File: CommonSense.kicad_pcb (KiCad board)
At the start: 2 copper layers, 35 x 24 mm, 36 parts, among them J1 Conn_02x04_Counter_Clockwise, J2 Conn_01x02, J3 Conn_01x02, J5 Conn_ARM_SWD_TagConnect_TC203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, U1 NRF52810-QFAA-R7, U2 SHT41-AD1B-R2, Y1 ECS-.327-12.5-12R-TR, Y2 ABM11W-32.0000MHZ-7-D1X-T3

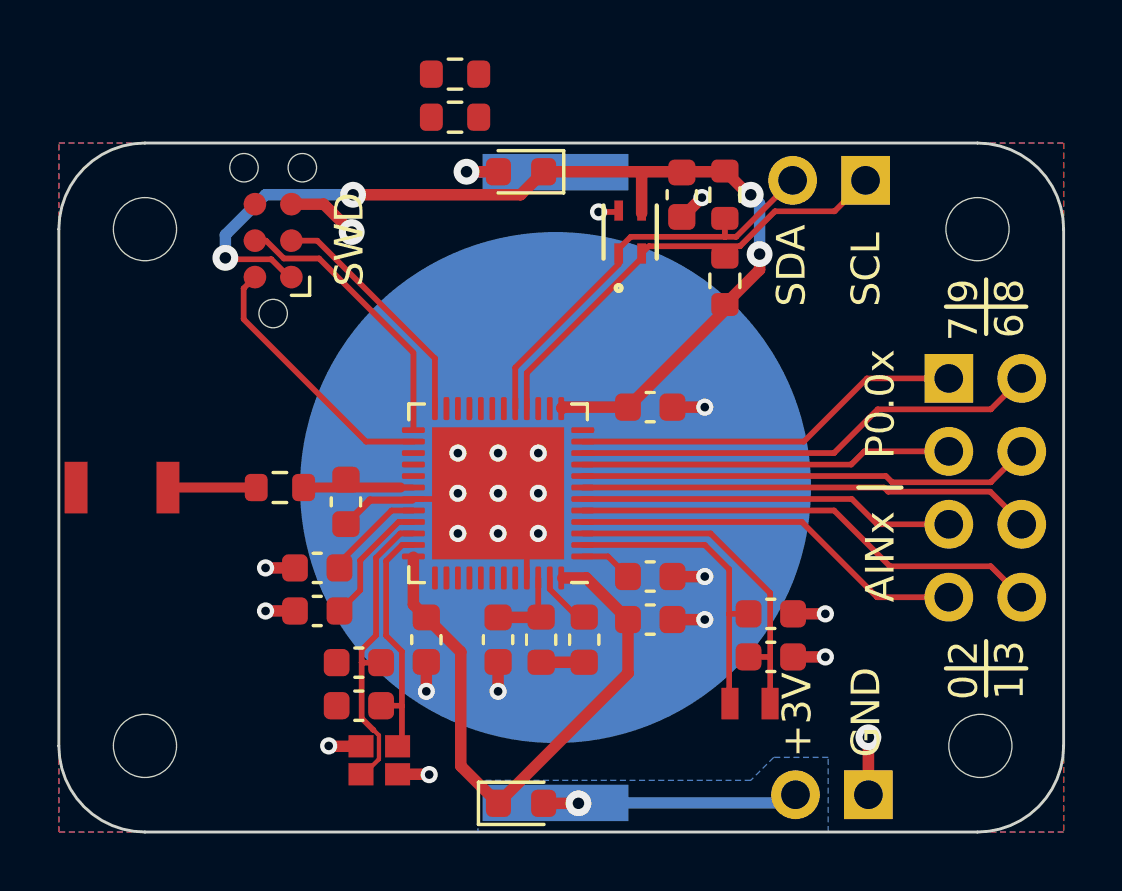
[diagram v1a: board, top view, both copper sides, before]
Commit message: Add additional 1u bypass capacitor
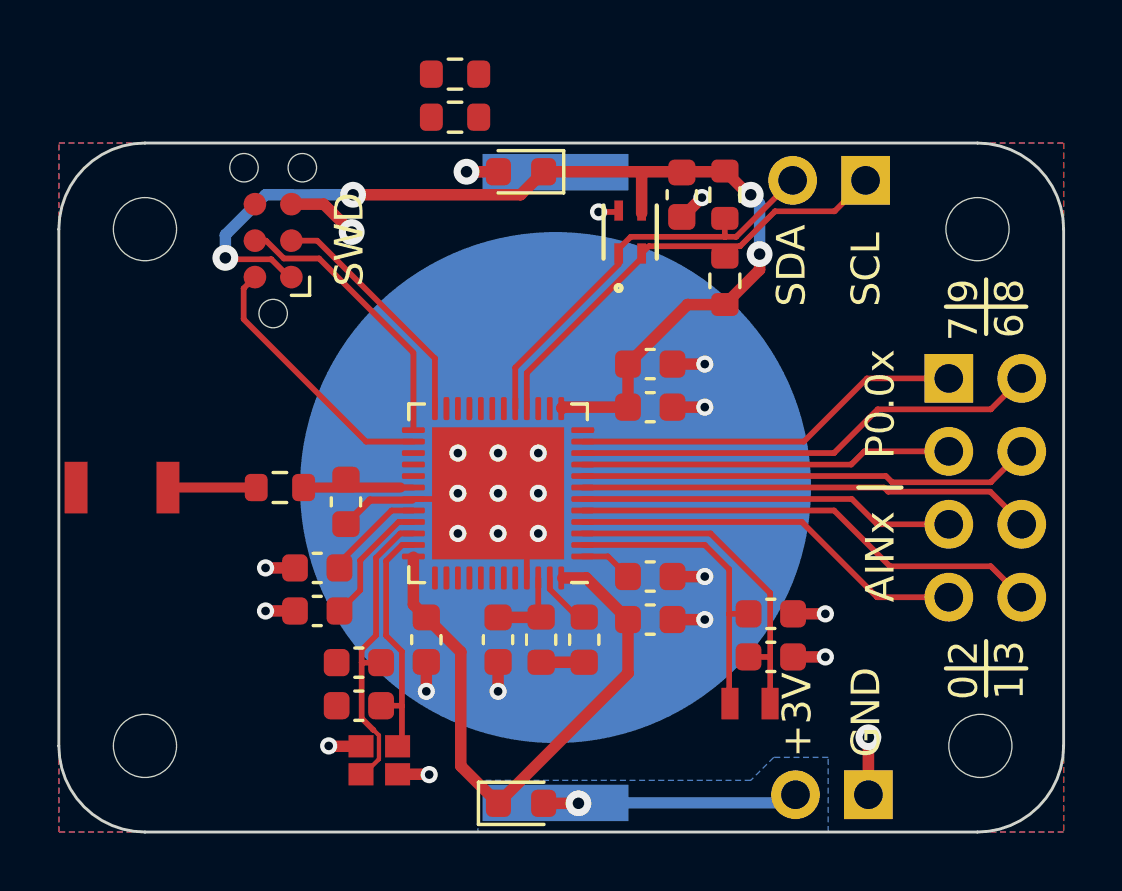
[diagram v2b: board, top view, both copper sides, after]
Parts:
- added C14: 1u, Capacitor_SMD:C_0603_1608Metric, F.Cu at (156.6, 63.7)
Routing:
- net GND: track 25.8 -> 26.9 mm, vias 24 -> 25
- net +3V0: track 57.1 -> 57.9 mm
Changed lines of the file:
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@@
+  )
+  (footprint "Capacitor_SMD:C_0603_1608Metric" (layer "F.Cu")
+    (at 156.6 63.7 180)
+    (descr "Capacitor SMD 0603 (1608 Metric), square (rectangular) end terminal, IPC_7351 nominal, (Body size source: IPC-SM-782 page 76, https://www.pcb-3d.com/wordpress/wp-content/uploads/ipc-sm-782a_amendment_1_and_2.pdf), generated with kicad-footprint-generator")
+    (tags "capacitor")
+    (property "Sheetfile" "CommonSense.kicad_sch")
+    (property "Sheetname" "")
+    (property "ki_description" "Unpolarized capacitor")
+    (property "ki_keywords" "cap capacitor")
+    (attr smd)
+    (fp_text reference "C14" (at 0 -1.43) (layer "F.SilkS") hide
+        (effects (font (size 1 1) (thickness 0.15)))
+    )
+    (fp_text value "1u" (at 0 1.43) (layer "F.Fab") hide
+        (effects (font (size 1 1) (thickness 0.15)))
+    )
+    (fp_text user "${REFERENCE}" (at 0 0) (layer "F.Fab") hide
+        (effects (font (size 0.4 0.4) (thickness 0.06)))
+    )
+    (fp_line (start -0.14058 -0.51) (end 0.14058 -0.51)
+      (stroke (width 0.12) (type solid)) (layer "F.SilkS"))
+    (fp_line (start -0.14058 0.51) (end 0.14058 0.51)
+      (stroke (width 0.12) (type solid)) (layer "F.SilkS"))
+    (fp_line (start -1.48 -0.73) (end 1.48 -0.73)
+      (stroke (width 0.05) (type solid)) (layer "F.CrtYd"))
+    (fp_line (start -1.48 0.73) (end -1.48 -0.73)
+      (stroke (width 0.05) (type solid)) (layer "F.CrtYd"))
+    (fp_line (start 1.48 -0.73) (end 1.48 0.73)
+      (stroke (width 0.05) (type solid)) (layer "F.CrtYd"))
+    (fp_line (start 1.48 0.73) (end -1.48 0.73)
+      (stroke (width 0.05) (type solid)) (layer "F.CrtYd"))
+    (fp_line (start -0.8 -0.4) (end 0.8 -0.4)
+      (stroke (width 0.1) (type solid)) (layer "F.Fab"))
+    (fp_line (start -0.8 0.4) (end -0.8 -0.4)
+      (stroke (width 0.1) (type solid)) (layer "F.Fab"))
+    (fp_line (start 0.8 -0.4) (end 0.8 0.4)
+      (stroke (width 0.1) (type solid)) (layer "F.Fab"))
+    (fp_line (start 0.8 0.4) (end -0.8 0.4)
+      (stroke (width 0.1) (type solid)) (layer "F.Fab"))
+    (pad "1" smd roundrect (at -0.775 0 180) (size 0.9 0.95) (layers "F.Cu" "F.Paste" "F.Mask") (roundrect_rratio 0.25)
+      (net 2 "GND") (pintype "passive"))
+    (pad "2" smd roundrect (at 0.775 0 180) (size 0.9 0.95) (layers "F.Cu" "F.Paste" "F.Mask") (roundrect_rratio 0.25)
+      (net 50 "+3V0") (pintype "passive"))
+    (model "${KICAD6_3DMODEL_DIR}/Capacitor_SMD.3dshapes/C_0603_1608Metric.wrl"
+      (offset (xyz 0 0 0))
+      (scale (xyz 1 1 1))
+      (rotate (xyz 0 0 0))
+    )
   )
   (footprint "Capacitor_SMD:C_0603_1608Metric" (layer "F.Cu")
@@
   (segment (start 161.575 73.9) (end 162.7 73.9) (width 0.4) (layer "F.Cu") (net 2))
   (segment (start 155.45305 58.4) (end 155.49995 58.3531) (width 0.2) (layer "F.Cu") (net 2))
+  (segment (start 157.375 63.7) (end 158.5 63.7) (width 0.4) (layer "F.Cu") (net 2))
   (segment (start 157.725 58.575) (end 158.4 57.9) (width 0.4) (layer "F.Cu") (net 2))
   (segment (start 145.413 77.013) (end 145.4 77) (width 0.4) (layer "F.Cu") (net 2))
@@
   (via (at 158.5 71.1) (size 0.6) (drill 0.3) (layers "F.Cu" "B.Cu") (net 2))
   (via (at 146.2 59.1) (size 0.9) (drill 0.4) (layers "F.Cu" "B.Cu") (net 2))
+  (via (at 158.5 63.7) (size 0.6) (drill 0.3) (layers "F.Cu" "B.Cu") (net 2))
   (via (at 148.9 78) (size 0.6) (drill 0.3) (layers "F.Cu" "B.Cu") (net 2))
   (via (at 149.9 68.2) (size 0.6) (drill 0.3) (layers "F.Cu" "B.Cu") (net 2))
@@
   (segment (start 153.285 57) (end 153.3 57.015) (width 0.4) (layer "B.Cu") (net 49))
   (segment (start 153.3 78.985) (end 161.375 78.985) (width 0.4) (layer "B.Cu") (net 49))
+  (segment (start 153.55 65.2) (end 153.527 65.223) (width 0.4) (layer "F.Cu") (net 50))
   (segment (start 143.401852 60.0493) (end 141.8493 60.0493) (width 0.2) (layer "F.Cu") (net 50))
   (segment (start 148.35 72.075) (end 148.35 70.427) (width 0.4) (layer "F.Cu") (net 50))
   (segment (start 160.409948 60.415052) (end 159.2 61.625) (width 0.4) (layer "F.Cu") (net 50))
+  (segment (start 155.825 63.7) (end 155.825 65.2) (width 0.4) (layer "F.Cu") (net 50))
+  (segment (start 153.527 65.223) (end 153.527 65.25) (width 0.4) (layer "F.Cu") (net 50))
   (segment (start 156.3 57) (end 159.175 57) (width 0.4) (layer "F.Cu") (net 50))
   (segment (start 154.375 71.15) (end 153.552 71.15) (width 0.4) (layer "F.Cu") (net 50))
+  (segment (start 159.2 61.625) (end 157.9 61.625) (width 0.4) (layer "F.Cu") (net 50))
   (segment (start 160.026642 57.801642) (end 159.2 56.975) (width 0.4) (layer "F.Cu") (net 50))
   (segment (start 156.3001 58.4531) (end 156.3001 57.0001) (width 0.4) (layer "F.Cu") (net 50))
   (segment (start 150 77.7) (end 150 73.725) (width 0.4) (layer "F.Cu") (net 50))
-  (segment (start 159.2 61.625) (end 159.2 61.825) (width 0.4) (layer "F.Cu") (net 50))
-  (segment (start 153.55 65.2) (end 153.527 65.223) (width 0.4) (layer "F.Cu") (net 50))
   (segment (start 148.8 72.525) (end 148.35 72.075) (width 0.4) (layer "F.Cu") (net 50))
   (segment (start 155.825 74.475) (end 155.825 72.6) (width 0.4) (layer "F.Cu") (net 50))
@@
   (segment (start 156.3001 57.0001) (end 156.3 57) (width 0.4) (layer "F.Cu") (net 50))
   (segment (start 152.8875 57) (end 156.3 57) (width 0.4) (layer "F.Cu") (net 50))
+  (segment (start 157.9 61.625) (end 155.825 63.7) (width 0.4) (layer "F.Cu") (net 50))
   (segment (start 160.101642 57.801642) (end 160.026642 57.801642) (width 0.4) (layer "F.Cu") (net 50))
-  (segment (start 159.2 61.825) (end 155.825 65.2) (width 0.4) (layer "F.Cu") (net 50))
   (segment (start 144.022552 60.67) (end 143.401852 60.0493) (width 0.2) (layer "F.Cu") (net 50))
   (segment (start 146.247897 57.802) (end 152.0855 57.802) (width 0.4) (layer "F.Cu") (net 50))
   (segment (start 152.0855 57.802) (end 152.8875 57) (width 0.4) (layer "F.Cu") (net 50))
-  (segment (start 155.825 65.2) (end 153.55 65.2) (width 0.4) (layer "F.Cu") (net 50))
   (segment (start 159.175 57) (end 159.2 56.975) (width 0.4) (layer "F.Cu") (net 50))
-  (segment (start 153.527 65.223) (end 153.527 65.25) (width 0.4) (layer "F.Cu") (net 50))
   (segment (start 150 73.725) (end 148.8 72.525) (width 0.4) (layer "F.Cu") (net 50))
   (segment (start 141.8493 60.0493) (end 141.8 60) (width 0.2) (layer "F.Cu") (net 50))
@@
   (segment (start 155.825 72.6) (end 154.375 71.15) (width 0.4) (layer "F.Cu") (net 50))
   (segment (start 151.3 79) (end 155.825 74.475) (width 0.4) (layer "F.Cu") (net 50))
+  (segment (start 155.825 65.2) (end 153.55 65.2) (width 0.4) (layer "F.Cu") (net 50))
   (via (at 160.409948 59.869216) (size 0.9) (drill 0.4) (layers "F.Cu" "B.Cu") (net 50))
   (via (at 160.101642 57.801642) (size 0.9) (drill 0.4) (layers "F.Cu" "B.Cu") (net 50))

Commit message: Route LED and fix silk screen warnings
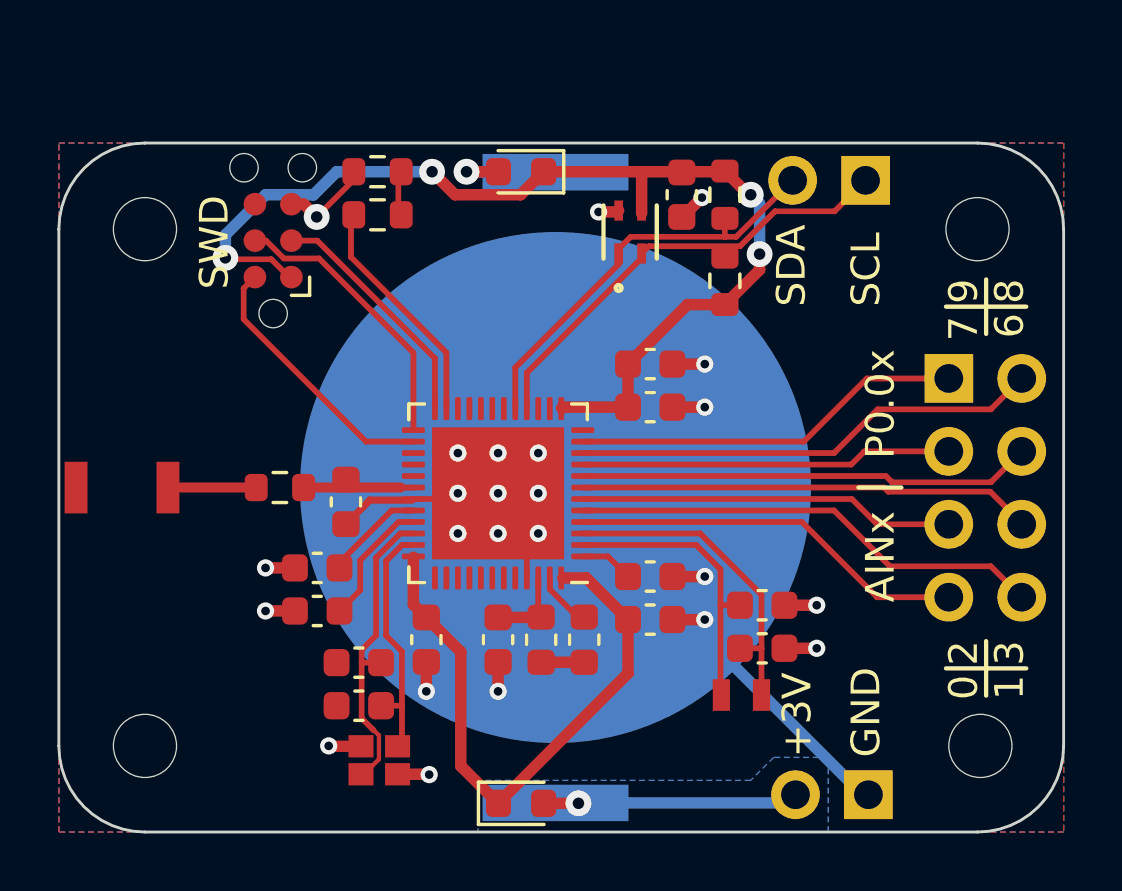
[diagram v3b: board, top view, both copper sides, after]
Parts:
- moved D1 4.34 mm to (147.1, 57.0)
- moved R1 4.34 mm to (147.1, 58.5)
- moved C1 0.42 mm to (160.5, 72.1)
- moved C2 0.42 mm to (160.5, 73.6)
- moved Y1 0.42 mm to (159.8, 75.2)
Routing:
- net GND: track 26.9 -> 40.9 mm, vias 25 -> 24
- net /STATUS_LED: track 0.00 -> 8.13 mm
- net /LED_RES: track 0.00 -> 1.50 mm
- net +3V0: track 57.9 -> 58.5 mm
- net /XL2: track 12.0 -> 11.4 mm
- net /XL1: track 10.8 -> 10.2 mm

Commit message: Add vias to avoid islands
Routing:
- net GND: vias 24 -> 33
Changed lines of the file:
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@@
   (segment (start 157.375 65.2) (end 158.5 65.2) (width 0.4) (layer "F.Cu") (net 2))
   (segment (start 146.175 57.380137) (end 144.980937 58.5742) (width 0.2) (layer "F.Cu") (net 2))
+  (via (at 144.8 61.7) (size 0.6) (drill 0.3) (layers "F.Cu" "B.Cu") (free) (net 2))
   (via (at 151.3 69.6) (size 0.6) (drill 0.3) (layers "F.Cu" "B.Cu") (net 2))
+  (via (at 138.9 62.4) (size 0.6) (drill 0.3) (layers "F.Cu" "B.Cu") (free) (net 2))
   (via (at 158.5 71.1) (size 0.6) (drill 0.3) (layers "F.Cu" "B.Cu") (net 2))
   (via (at 144.980937 58.5742) (size 0.9) (drill 0.4) (layers "F.Cu" "B.Cu") (net 2))
+  (via (at 149.4 61.3) (size 0.6) (drill 0.3) (layers "F.Cu" "B.Cu") (net 2))
+  (via (at 154.1 63.8) (size 0.6) (drill 0.3) (layers "F.Cu" "B.Cu") (net 2))
   (via (at 158.5 63.7) (size 0.6) (drill 0.3) (layers "F.Cu" "B.Cu") (net 2))
   (via (at 148.9 78) (size 0.6) (drill 0.3) (layers "F.Cu" "B.Cu") (net 2))
   (via (at 149.9 68.2) (size 0.6) (drill 0.3) (layers "F.Cu" "B.Cu") (net 2))
   (via (at 154.8 58.4) (size 0.6) (drill 0.3) (layers "F.Cu" "B.Cu") (net 2))
+  (via (at 157.5 60.7) (size 0.6) (drill 0.3) (layers "F.Cu" "B.Cu") (net 2))
   (via (at 149.9 66.8) (size 0.6) (drill 0.3) (layers "F.Cu" "B.Cu") (net 2))
+  (via (at 147 64.7) (size 0.6) (drill 0.3) (layers "F.Cu" "B.Cu") (net 2))
   (via (at 149.9 69.6) (size 0.6) (drill 0.3) (layers "F.Cu" "B.Cu") (net 2))
   (via (at 162.4 72.1) (size 0.6) (drill 0.3) (layers "F.Cu" "B.Cu") (net 2))
@@
   (via (at 145.4 77) (size 0.6) (drill 0.3) (layers "F.Cu" "B.Cu") (net 2))
   (via (at 143.2 72.3) (size 0.6) (drill 0.3) (layers "F.Cu" "B.Cu") (net 2))
+  (via (at 165.7 60.9) (size 0.6) (drill 0.3) (layers "F.Cu" "B.Cu") (free) (net 2))
   (via (at 151.3 66.8) (size 0.6) (drill 0.3) (layers "F.Cu" "B.Cu") (net 2))
   (via (at 148.8 75.1) (size 0.6) (drill 0.3) (layers "F.Cu" "B.Cu") (net 2))
+  (via (at 141.9 77.2) (size 0.6) (drill 0.3) (layers "F.Cu" "B.Cu") (free) (net 2))
   (via (at 143.2 70.8) (size 0.6) (drill 0.3) (layers "F.Cu" "B.Cu") (net 2))
   (via (at 158.4 57.9) (size 0.6) (drill 0.3) (layers "F.Cu" "B.Cu") (net 2))
+  (via (at 144.5 66.4) (size 0.6) (drill 0.3) (layers "F.Cu" "B.Cu") (free) (net 2))
   (via (at 152.7 66.8) (size 0.6) (drill 0.3) (layers "F.Cu" "B.Cu") (net 2))
   (via (at 152.7 69.6) (size 0.6) (drill 0.3) (layers "F.Cu" "B.Cu") (net 2))

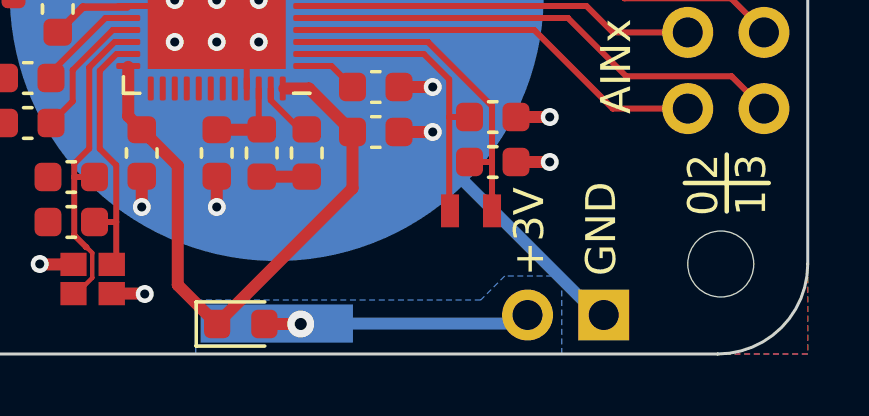
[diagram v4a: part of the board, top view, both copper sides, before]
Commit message: Move power pin header to properly align with I2C pin header
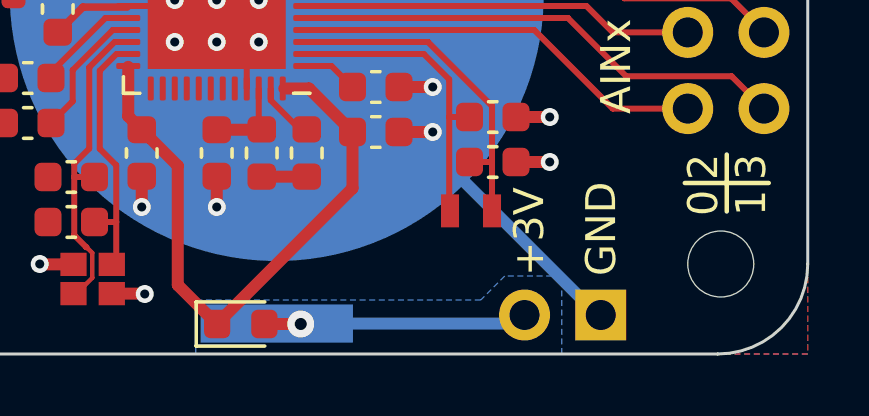
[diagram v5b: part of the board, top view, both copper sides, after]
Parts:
- moved J2 0.10 mm to (164.1, 78.7)
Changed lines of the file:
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@@
   )
   (footprint "Connector_PinHeader_2.54mm:PinHeader_1x02_P2.54mm_Vertical" locked (layer "F.Cu")
-    (at 164.2 78.7 -90)
+    (at 164.1 78.7 -90)
     (descr "Through hole straight pin header, 1x02, 2.54mm pitch, single row")
     (tags "Through hole pin header THT 1x02 2.54mm single row")
@@
   (via (at 152.7 69.6) (size 0.6) (drill 0.3) (layers "F.Cu" "B.Cu") (net 2))
   (segment (start 164 78.7) (end 153.3 68) (width 0.4) (layer "B.Cu") (net 2))
-  (segment (start 164.2 78.7) (end 164 78.7) (width 0.4) (layer "B.Cu") (net 2))
+  (segment (start 164.1 78.7) (end 164 78.7) (width 0.4) (layer "B.Cu") (net 2))
   (segment (start 159.048 75.198983) (end 159.048 72.1) (width 0.2) (layer "F.Cu") (net 3))
   (segment (start 159.725 72.1) (end 159.048 72.1) (width 0.2) (layer "F.Cu") (net 3))
@@
   (via (at 154.1 79) (size 0.9) (drill 0.4) (layers "F.Cu" "B.Cu") (net 49))
   (via (at 150.2 57) (size 0.9) (drill 0.4) (layers "F.Cu" "B.Cu") (net 49))
-  (segment (start 161.375 78.985) (end 161.66 78.7) (width 0.4) (layer "B.Cu") (net 49))
+  (segment (start 153.3 78.985) (end 161.275 78.985) (width 0.4) (layer "B.Cu") (net 49))
+  (segment (start 161.275 78.985) (end 161.56 78.7) (width 0.4) (layer "B.Cu") (net 49))
   (segment (start 150.2 57) (end 153.285 57) (width 0.4) (layer "B.Cu") (net 49))
   (segment (start 153.285 57) (end 153.3 57.015) (width 0.4) (layer "B.Cu") (net 49))
-  (segment (start 153.3 78.985) (end 161.375 78.985) (width 0.4) (layer "B.Cu") (net 49))
   (segment (start 153.55 65.2) (end 153.527 65.223) (width 0.4) (layer "F.Cu") (net 50))
   (segment (start 143.401852 60.0493) (end 141.8493 60.0493) (width 0.2) (layer "F.Cu") (net 50))
